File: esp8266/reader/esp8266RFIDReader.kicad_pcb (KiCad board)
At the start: 2 copper layers, 33.8 x 33 mm, 18 parts, among them J1 J1, J2 J2, U1 RFID_MODULE_125_KHZ

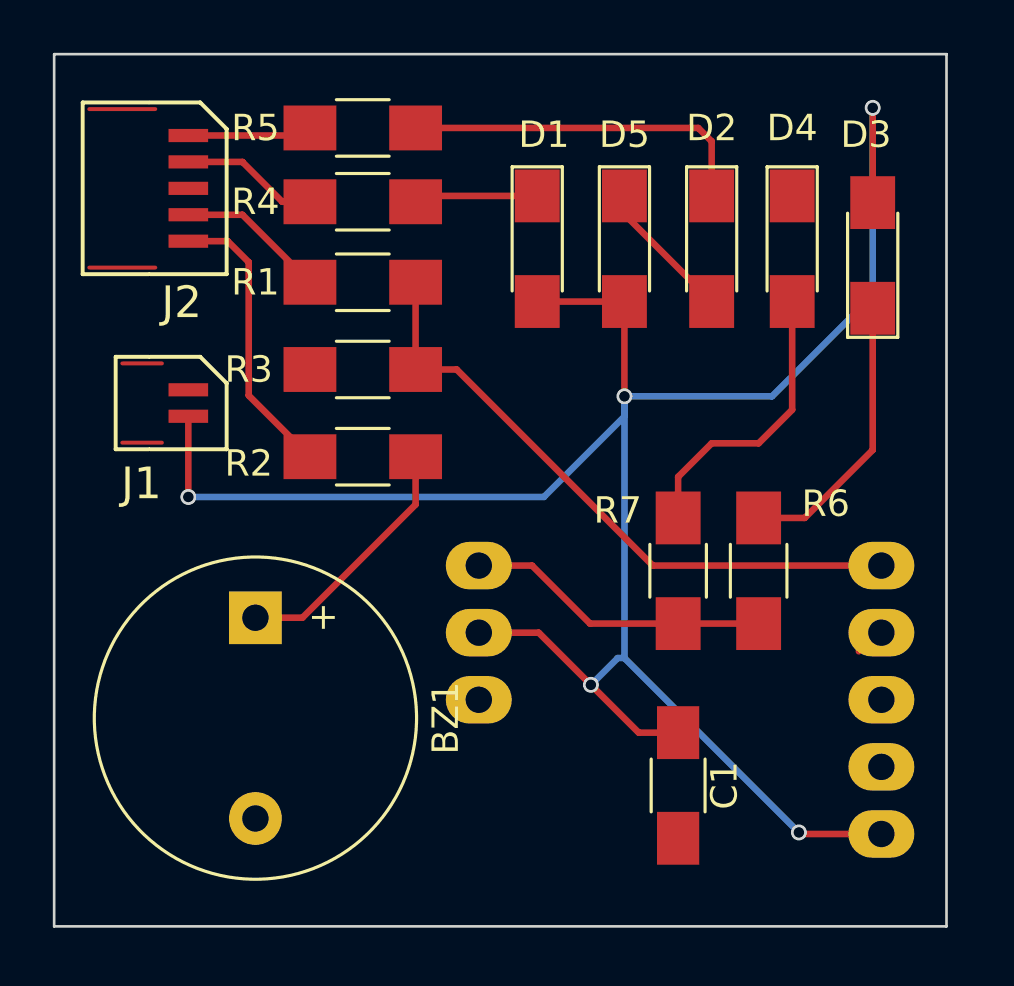
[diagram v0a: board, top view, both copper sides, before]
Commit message: Schematic and PCB for RFID control module.
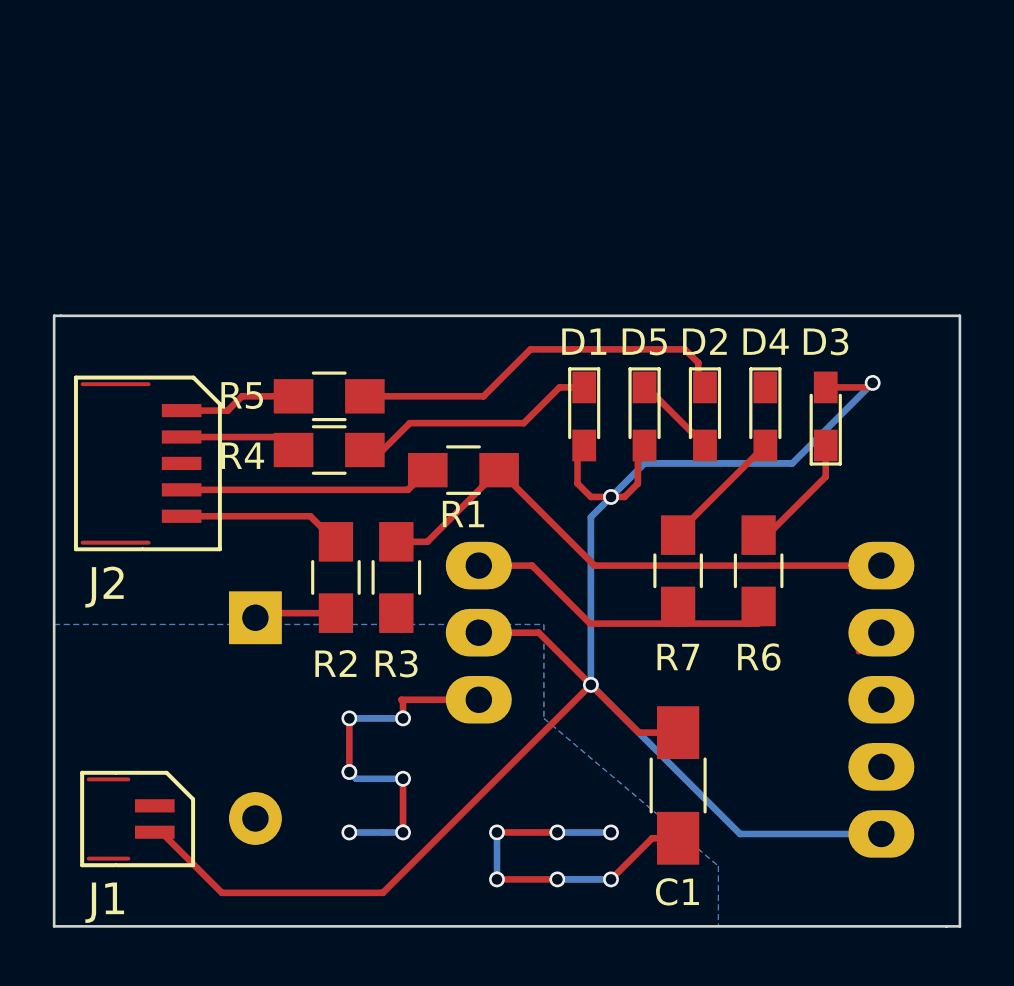
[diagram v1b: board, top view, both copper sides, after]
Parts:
- removed G***: LOGO, ml_logo:ML_Logo
- added ?: , ml_logo:ML_Logo, B.Cu at (77.7, 89.7)
- BZ1: moved to B.Cu
- D1, D2, D3, D4, D5: footprint LEDs:LED_1206_HandSoldering -> LEDs:LED_0603_HandSoldering
- R1, R2, R3, R4, R5, R6, R7: footprint Resistors_SMD:R_1206_HandSoldering -> Resistors_SMD:R_0805_HandSoldering
- moved J1 15.8 mm to (74.2, 103.9)
- moved J2 10.4 mm to (75.2, 90.4)
- moved R5 10.2 mm to (80.8, 87.9)
- moved R4 9.48 mm to (80.8, 89.9)
- moved R1 8.07 mm to (85.9, 90.7)
- moved R3 7.98 mm to (83.3, 94.7), turned to 90 degrees
- moved D1 6.59 mm to (90.4, 88.6)
- moved D4 6.43 mm to (97.3, 88.6)
- moved D5 6.40 mm to (92.7, 88.6)
- moved D2 6.36 mm to (95.0, 88.6)
- moved D3 6.35 mm to (99.6, 88.6)
- moved R2 4.68 mm to (81.0, 94.7), turned to 90 degrees
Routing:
- net GND: track 0.00 -> 27.5 mm, vias 0 -> 12
- net +5V: track 83.6 -> 70.0 mm, vias 5 -> 3
- net Net-(D4-Pad2): track 11.0 -> 4.76 mm
- net Net-(D3-Pad1): track 10.7 -> 4.64 mm
- net Net-(BZ1-Pad1): track 9.65 -> 3.59 mm
- net Buzzer: track 10.9 -> 6.24 mm
- net Net-(J2-Pad4): track 5.66 -> 9.63 mm
- net Net-(D1-Pad1): track 5.17 -> 9.03 mm
- net Net-(R1-Pad1): track 24.0 -> 21.0 mm
- net Net-(D2-Pad2): track 5.73 -> 3.20 mm
- net LED_CONFIRM: track 5.61 -> 4.44 mm
- net Net-(D2-Pad1): track 13.5 -> 14.5 mm
- added copper zone on B.Cu, net GND
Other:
- board size 33.8 x 33 mm -> 34.3 x 23.1 mm
- board text added: "ESP RFID Reader v1.0"
- board text removed: "ESP RFID Reader Module v1.0"
